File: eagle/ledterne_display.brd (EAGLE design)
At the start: 15 x 15 mm, 5 parts

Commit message: - Added possible routing (one layer only).
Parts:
- moved R3 8.05 mm to (7.50, 12.5), flipped to the top, turned to 0 degrees
- moved JP1 7.16 mm to (7.85, 3.19)
- moved R1 5.89 mm to (3.00, 10.0), flipped to the top, turned to 90 degrees
- moved R2 2.34 mm to (1.50, 6.00), flipped to the top
- moved LED1 2.18 mm to (8.00, 8.50), turned to 0 degrees
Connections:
- new net N$4: JP1.1, R1.2
- new net N$5: JP1.2, R2.2
- new net N$6: JP1.3, R3.2
- net GND: now also JP1.4
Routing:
- net N$4: track 0.00 -> 39.2 mm
- net N$6: track 0.00 -> 22.1 mm
- net N$5: track 0.00 -> 6.94 mm
- net GND: track 3.08 -> 7.66 mm
- net N$3: track 7.76 -> 3.86 mm, vias 1 -> 0
- net N$1: track 5.09 -> 2.70 mm, vias 1 -> 0
- net N$2: track 4.15 -> 3.65 mm, vias 1 -> 0
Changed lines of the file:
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@@
 <setting verticaltext="up"/>
 </settings>
-<grid distance="0.05" unitdist="inch" unit="mm" style="lines" multiple="1" display="yes" altdistance="0.025" altunitdist="inch" altunit="mm"/>
+<grid distance="1" unitdist="mm" unit="mm" style="lines" multiple="1" display="yes" altdistance="0.5" altunitdist="mm" altunit="mm"/>
 <layers>
 <layer number="1" name="Top" color="4" fill="1" visible="yes" active="yes"/>
@@
 <layer number="23" name="tOrigins" color="15" fill="1" visible="yes" active="yes"/>
 <layer number="24" name="bOrigins" color="15" fill="1" visible="yes" active="yes"/>
-<layer number="25" name="tNames" color="7" fill="1" visible="no" active="yes"/>
+<layer number="25" name="tNames" color="7" fill="1" visible="yes" active="yes"/>
 <layer number="26" name="bNames" color="7" fill="1" visible="yes" active="yes"/>
-<layer number="27" name="tValues" color="7" fill="1" visible="no" active="yes"/>
+<layer number="27" name="tValues" color="7" fill="1" visible="yes" active="yes"/>
 <layer number="28" name="bValues" color="7" fill="1" visible="yes" active="yes"/>
 <layer number="29" name="tStop" color="7" fill="3" visible="no" active="yes"/>
@@
 </autorouter>
 <elements>
-<element name="LED1" library="led-rgb" package="SMD_5252" value="RGB-5252" x="7.62" y="6.35" rot="R270"/>
-<element name="R1" library="resistor" package="R0805" value="" x="7.62" y="6.35" rot="MR270"/>
-<element name="R2" library="resistor" package="R0805" value="" x="3.81" y="6.35" rot="MR270"/>
-<element name="R3" library="resistor" package="R0805" value="" x="12.7" y="6.35" rot="MR270"/>
-<element name="JP1" library="pinhead" package="1X04" value="" x="6.35" y="-3.81"/>
+<element name="LED1" library="led-rgb" package="SMD_5252" value="RGB-5252" x="8" y="8.5"/>
+<element name="R1" library="resistor" package="R0805" value="" x="3" y="10" rot="R90"/>
+<element name="R2" library="resistor" package="R0805" value="" x="1.5" y="6" rot="R270"/>
+<element name="R3" library="resistor" package="R0805" value="" x="7.5" y="12.5"/>
+<element name="JP1" library="pinhead" package="1X04" value="" x="7.85" y="3.19"/>
 </elements>
 <signals>
@@
 <contactref element="R1" pad="1"/>
 <contactref element="LED1" pad="P2"/>
-<wire x1="7.62" y1="7.3" x2="7.62" y2="10.795" width="0.4064" layer="16"/>
-<via x="7.62" y="10.795" extent="1-16" drill="0.6" shape="square"/>
-<wire x1="7.62" y1="10.795" x2="7.62" y2="9.2" width="0.4064" layer="1"/>
+<wire x1="3" y1="9.05" x2="3" y2="8.5" width="0.4064" layer="1"/>
+<wire x1="3" y1="8.5" x2="5.15" y2="8.5" width="0.4064" layer="1"/>
 </signal>
 <signal name="N$2">
 <contactref element="R2" pad="1"/>
 <contactref element="LED1" pad="P3"/>
-<wire x1="3.81" y1="7.3" x2="3.81" y2="9.16" width="0.4064" layer="16"/>
-<via x="3.81" y="9.16" extent="1-16" drill="0.6" shape="square"/>
-<wire x1="3.81" y1="9.16" x2="3.85" y2="9.2" width="0.4064" layer="1"/>
-<wire x1="3.85" y1="9.2" x2="6.08" y2="9.2" width="0.4064" layer="1"/>
+<wire x1="1.5" y1="6.95" x2="4.65" y2="6.95" width="0.4064" layer="1"/>
+<wire x1="4.65" y1="6.95" x2="5.15" y2="6.96" width="0.4064" layer="1"/>
 </signal>
 <signal name="N$3">
 <contactref element="R3" pad="1"/>
 <contactref element="LED1" pad="P1"/>
-<wire x1="12.7" y1="7.3" x2="10.43" y2="11.7" width="0.4064" layer="16"/>
-<wire x1="10.43" y1="11.7" x2="9.16" y2="9.2" width="0.4064" layer="1"/>
-<via x="10.43" y="11.7" extent="1-16" drill="0.6" shape="square"/>
+<wire x1="6.55" y1="12.5" x2="5.15" y2="12.5" width="0.4064" layer="1"/>
+<wire x1="5.15" y1="12.5" x2="5.15" y2="10.04" width="0.4064" layer="1"/>
 </signal>
 <signal name="GND">
@@
 <contactref element="LED1" pad="P5"/>
 <contactref element="LED1" pad="P6"/>
-<wire x1="6.08" y1="3.5" x2="7.62" y2="3.5" width="0.4064" layer="1"/>
-<wire x1="7.62" y1="3.5" x2="9.16" y2="3.5" width="0.4064" layer="1"/>
+<contactref element="JP1" pad="4"/>
+<wire x1="10.85" y1="6.96" x2="11.66" y2="6.96" width="0.4064" layer="1"/>
+<wire x1="11.66" y1="6.96" x2="11.66" y2="3.19" width="0.4064" layer="1"/>
+<wire x1="10.85" y1="6.96" x2="10.85" y2="8.5" width="0.4064" layer="1"/>
+<wire x1="10.85" y1="8.5" x2="10.85" y2="10.04" width="0.4064" layer="1"/>
+</signal>
+<signal name="N$4">
+<contactref element="JP1" pad="1"/>
+<contactref element="R1" pad="2"/>
+<wire x1="3" y1="10.95" x2="3" y2="14" width="0.4064" layer="1"/>
+<wire x1="3" y1="14" x2="14" y2="14" width="0.4064" layer="1"/>
+<wire x1="14" y1="14" x2="14" y2="1" width="0.4064" layer="1"/>
+<wire x1="14" y1="1" x2="4.04" y2="1" width="0.4064" layer="1"/>
+<wire x1="4.04" y1="1" x2="4.04" y2="3.19" width="0.4064" layer="1"/>
+</signal>
+<signal name="N$5">
+<contactref element="JP1" pad="2"/>
+<contactref element="R2" pad="2"/>
+<wire x1="1.5" y1="5.05" x2="6.58" y2="5.05" width="0.4064" layer="1"/>
+<wire x1="6.58" y1="5.05" x2="6.58" y2="3.19" width="0.4064" layer="1"/>
+</signal>
+<signal name="N$6">
+<contactref element="JP1" pad="3"/>
+<contactref element="R3" pad="2"/>
+<wire x1="8.45" y1="12.5" x2="13.5" y2="12.5" width="0.4064" layer="1"/>
+<wire x1="13.5" y1="12.5" x2="13.5" y2="1.5" width="0.4064" layer="1"/>
+<wire x1="13.5" y1="1.5" x2="9.12" y2="1.5" width="0.4064" layer="1"/>
+<wire x1="9.12" y1="1.5" x2="9.12" y2="3.19" width="0.4064" layer="1"/>
 </signal>
 </signals>

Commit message: Assign net names to the LED inputs
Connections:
- net N$4 renamed LED_R
- net N$5 renamed LED_G
- net N$6 renamed LED_B
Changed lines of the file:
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@@
 <wire x1="10.85" y1="8.5" x2="10.85" y2="10.04" width="0.4064" layer="1"/>
 </signal>
-<signal name="N$4">
+<signal name="LED_R">
 <contactref element="JP1" pad="1"/>
 <contactref element="R1" pad="2"/>
@@
 <wire x1="4.04" y1="1" x2="4.04" y2="3.19" width="0.4064" layer="1"/>
 </signal>
-<signal name="N$5">
+<signal name="LED_G">
 <contactref element="JP1" pad="2"/>
 <contactref element="R2" pad="2"/>
@@
 <wire x1="6.58" y1="5.05" x2="6.58" y2="3.19" width="0.4064" layer="1"/>
 </signal>
-<signal name="N$6">
+<signal name="LED_B">
 <contactref element="JP1" pad="3"/>
 <contactref element="R3" pad="2"/>

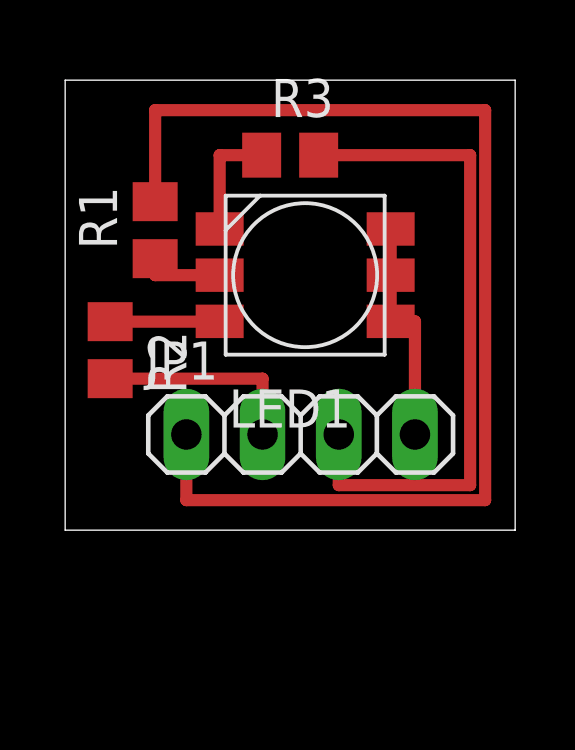
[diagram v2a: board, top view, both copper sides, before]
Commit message: Update routing to be more compact
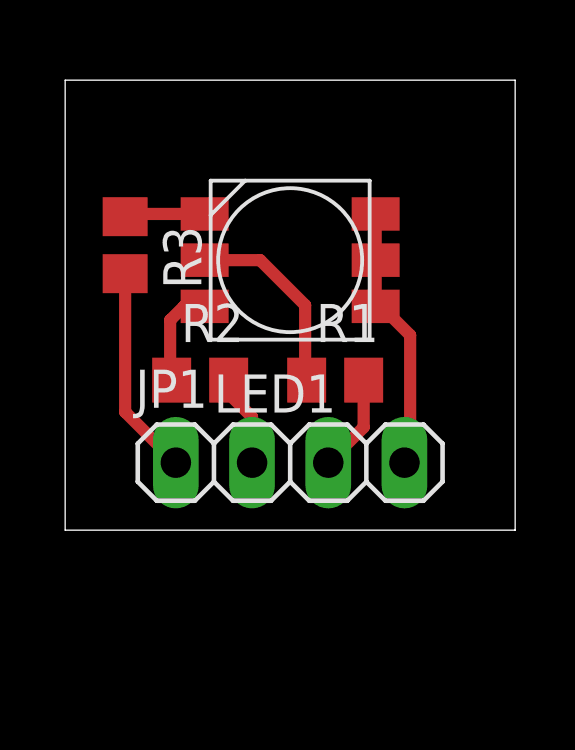
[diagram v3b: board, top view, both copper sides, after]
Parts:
- moved R1 7.81 mm to (9.00, 5.00), turned to 0 degrees
- moved R3 6.26 mm to (2.00, 9.50), turned to 270 degrees
- moved R2 3.16 mm to (4.50, 5.00), turned to 0 degrees
- moved JP1 1.00 mm to (7.50, 2.25)
- moved LED1 0.71 mm to (7.50, 9.00)
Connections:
- net LED_B: now also JP1.1; no longer JP1.3
- net LED_R: now also JP1.3; no longer JP1.1
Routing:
- net LED_R: track 39.2 -> 3.24 mm
- net LED_B: track 22.1 -> 7.00 mm
- net LED_G: track 6.94 -> 3.07 mm
- net N$1: track 2.70 -> 6.49 mm
- net GND: track 7.66 -> 8.96 mm
- net N$3: track 3.86 -> 2.69 mm
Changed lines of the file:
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@@
 <setting verticaltext="up"/>
 </settings>
-<grid distance="1" unitdist="mm" unit="mm" style="lines" multiple="1" display="yes" altdistance="0.5" altunitdist="mm" altunit="mm"/>
+<grid distance="1" unitdist="mm" unit="mm" style="lines" multiple="1" display="no" altdistance="0.25" altunitdist="mm" altunit="mm"/>
 <layers>
 <layer number="1" name="Top" color="4" fill="1" visible="yes" active="yes"/>
@@
 <layer number="42" name="bRestrict" color="1" fill="10" visible="yes" active="yes"/>
 <layer number="43" name="vRestrict" color="2" fill="10" visible="yes" active="yes"/>
-<layer number="44" name="Drills" color="7" fill="1" visible="yes" active="yes"/>
+<layer number="44" name="Drills" color="7" fill="1" visible="no" active="yes"/>
 <layer number="45" name="Holes" color="7" fill="1" visible="yes" active="yes"/>
 <layer number="46" name="Milling" color="3" fill="1" visible="yes" active="yes"/>
@@
 </autorouter>
 <elements>
-<element name="LED1" library="led-rgb" package="SMD_5252" value="RGB-5252" x="8" y="8.5"/>
-<element name="R1" library="resistor" package="R0805" value="" x="3" y="10" rot="R90"/>
-<element name="R2" library="resistor" package="R0805" value="" x="1.5" y="6" rot="R270"/>
-<element name="R3" library="resistor" package="R0805" value="" x="7.5" y="12.5"/>
-<element name="JP1" library="pinhead" package="1X04" value="" x="7.85" y="3.19"/>
+<element name="LED1" library="led-rgb" package="SMD_5252" value="RGB-5252" x="7.5" y="9"/>
+<element name="R1" library="resistor" package="R0805" value="" x="9" y="5"/>
+<element name="R2" library="resistor" package="R0805" value="" x="4.5" y="5"/>
+<element name="R3" library="resistor" package="R0805" value="" x="2" y="9.5" rot="R270"/>
+<element name="JP1" library="pinhead" package="1X04" value="" x="7.5" y="2.25"/>
 </elements>
 <signals>
@@
 <contactref element="R1" pad="1"/>
 <contactref element="LED1" pad="P2"/>
-<wire x1="3" y1="9.05" x2="3" y2="8.5" width="0.4064" layer="1"/>
-<wire x1="3" y1="8.5" x2="5.15" y2="8.5" width="0.4064" layer="1"/>
+<wire x1="4.65" y1="9" x2="6.5" y2="9" width="0.4064" layer="1"/>
+<wire x1="6.5" y1="9" x2="8" y2="7.5" width="0.4064" layer="1"/>
+<wire x1="8" y1="7.5" x2="8" y2="5.05" width="0.4064" layer="1"/>
+<wire x1="8" y1="5.05" x2="8.05" y2="5" width="0.4064" layer="1"/>
 </signal>
 <signal name="N$2">
 <contactref element="R2" pad="1"/>
 <contactref element="LED1" pad="P3"/>
-<wire x1="1.5" y1="6.95" x2="4.65" y2="6.95" width="0.4064" layer="1"/>
-<wire x1="4.65" y1="6.95" x2="5.15" y2="6.96" width="0.4064" layer="1"/>
+<wire x1="4.65" y1="7.46" x2="3.96" y2="7.46" width="0.4064" layer="1"/>
+<wire x1="3.96" y1="7.46" x2="3.5" y2="7" width="0.4064" layer="1"/>
+<wire x1="3.5" y1="7" x2="3.5" y2="5.05" width="0.4064" layer="1"/>
+<wire x1="3.5" y1="5.05" x2="3.55" y2="5" width="0.4064" layer="1"/>
 </signal>
 <signal name="N$3">
 <contactref element="R3" pad="1"/>
 <contactref element="LED1" pad="P1"/>
-<wire x1="6.55" y1="12.5" x2="5.15" y2="12.5" width="0.4064" layer="1"/>
-<wire x1="5.15" y1="12.5" x2="5.15" y2="10.04" width="0.4064" layer="1"/>
+<wire x1="4.65" y1="10.54" x2="2.09" y2="10.54" width="0.4064" layer="1"/>
+<wire x1="2.09" y1="10.54" x2="2" y2="10.45" width="0.4064" layer="1"/>
 </signal>
 <signal name="GND">
@@
 <contactref element="LED1" pad="P6"/>
 <contactref element="JP1" pad="4"/>
-<wire x1="10.85" y1="6.96" x2="11.66" y2="6.96" width="0.4064" layer="1"/>
-<wire x1="11.66" y1="6.96" x2="11.66" y2="3.19" width="0.4064" layer="1"/>
-<wire x1="10.85" y1="6.96" x2="10.85" y2="8.5" width="0.4064" layer="1"/>
-<wire x1="10.85" y1="8.5" x2="10.85" y2="10.04" width="0.4064" layer="1"/>
+<wire x1="10.35" y1="9" x2="10.35" y2="10.54" width="0.4064" layer="1"/>
+<wire x1="10.35" y1="7.46" x2="10.35" y2="9" width="0.4064" layer="1"/>
+<wire x1="10.35" y1="7.46" x2="10.54" y2="7.46" width="0.4064" layer="1"/>
+<wire x1="10.54" y1="7.46" x2="11.5" y2="6.5" width="0.4064" layer="1"/>
+<wire x1="11.5" y1="6.5" x2="11.5" y2="2.44" width="0.4064" layer="1"/>
+<wire x1="11.5" y1="2.44" x2="11.31" y2="2.25" width="0.4064" layer="1"/>
 </signal>
 <signal name="LED_R">
-<contactref element="JP1" pad="1"/>
 <contactref element="R1" pad="2"/>
-<wire x1="3" y1="10.95" x2="3" y2="14" width="0.4064" layer="1"/>
-<wire x1="3" y1="14" x2="14" y2="14" width="0.4064" layer="1"/>
-<wire x1="14" y1="14" x2="14" y2="1" width="0.4064" layer="1"/>
-<wire x1="14" y1="1" x2="4.04" y2="1" width="0.4064" layer="1"/>
-<wire x1="4.04" y1="1" x2="4.04" y2="3.19" width="0.4064" layer="1"/>
+<contactref element="JP1" pad="3"/>
+<wire x1="9.95" y1="5" x2="9.95" y2="3.43" width="0.4064" layer="1"/>
+<wire x1="9.95" y1="3.43" x2="8.77" y2="2.25" width="0.4064" layer="1"/>
 </signal>
 <signal name="LED_G">
 <contactref element="JP1" pad="2"/>
 <contactref element="R2" pad="2"/>
-<wire x1="1.5" y1="5.05" x2="6.58" y2="5.05" width="0.4064" layer="1"/>
-<wire x1="6.58" y1="5.05" x2="6.58" y2="3.19" width="0.4064" layer="1"/>
+<wire x1="6.23" y1="2.25" x2="6.23" y2="3.77" width="0.4064" layer="1"/>
+<wire x1="6.23" y1="3.77" x2="5.5" y2="4.5" width="0.4064" layer="1"/>
+<wire x1="5.5" y1="4.5" x2="5.5" y2="4.95" width="0.4064" layer="1"/>
+<wire x1="5.5" y1="4.95" x2="5.45" y2="5" width="0.4064" layer="1"/>
 </signal>
 <signal name="LED_B">
-<contactref element="JP1" pad="3"/>
 <contactref element="R3" pad="2"/>
-<wire x1="8.45" y1="12.5" x2="13.5" y2="12.5" width="0.4064" layer="1"/>
-<wire x1="13.5" y1="12.5" x2="13.5" y2="1.5" width="0.4064" layer="1"/>
-<wire x1="13.5" y1="1.5" x2="9.12" y2="1.5" width="0.4064" layer="1"/>
-<wire x1="9.12" y1="1.5" x2="9.12" y2="3.19" width="0.4064" layer="1"/>
+<contactref element="JP1" pad="1"/>
+<wire x1="2" y1="8.55" x2="2" y2="3.94" width="0.4064" layer="1"/>
+<wire x1="2" y1="3.94" x2="3.69" y2="2.25" width="0.4064" layer="1"/>
 </signal>
 </signals>
